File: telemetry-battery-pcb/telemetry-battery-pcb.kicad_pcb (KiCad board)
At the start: 2 copper layers, 95 x 65 mm, 110 parts, among them J1 Network Connector, J2 STDC14, J3 CONN_360410_MZC, J4 DS18B20, J5 CONN_360410_MZC, Q1 NMOS, Q2 PMOS, Q4 NMOS, SW1 SW_Push, U1 LD39050PU33R, U2 STM32G474RBT6, U3 SN65HVD230, U4 LTC2944, U5 XR76208, U6 M24C02-WMN, U7 TPS1HTC30-Q1, U8 DS2484Q, Y1 8MHz

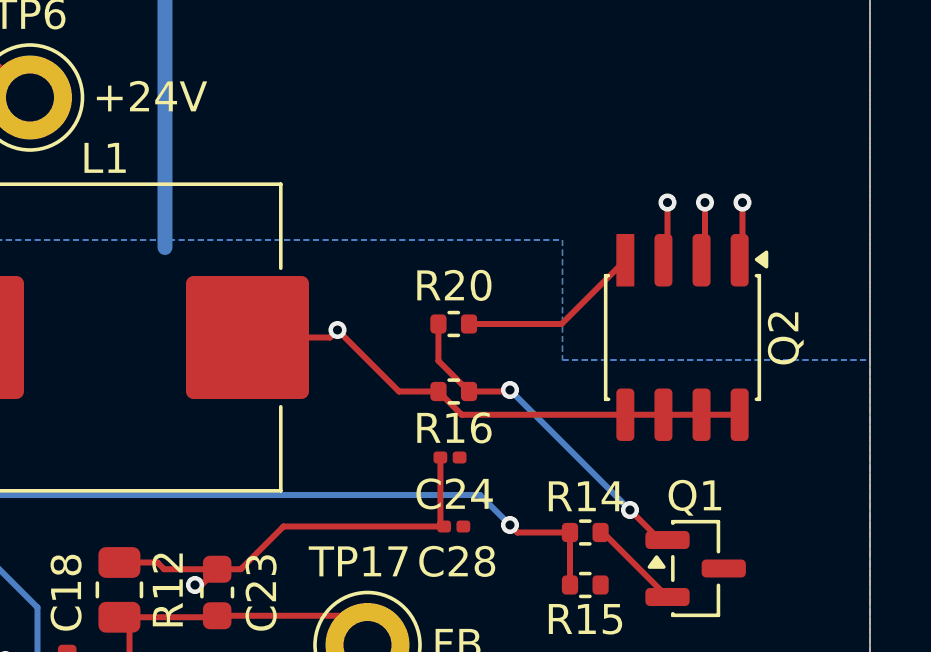
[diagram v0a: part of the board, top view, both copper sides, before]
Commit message: telemetry-battery-pcb: enlarge +5V net after coil
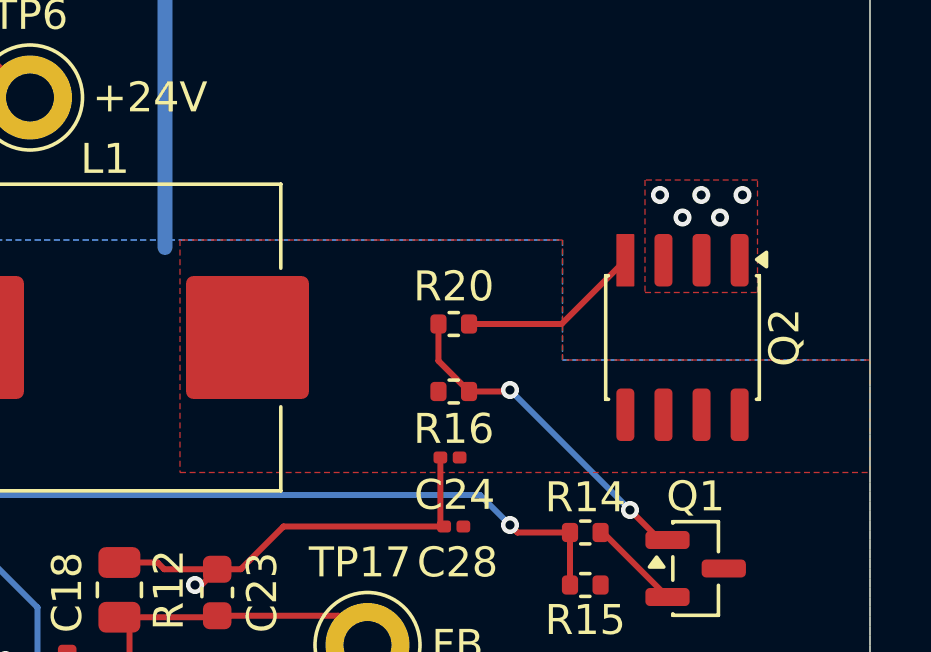
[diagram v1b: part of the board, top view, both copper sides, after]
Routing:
- net +5V: track 78.7 -> 62.7 mm, vias 4 -> 3
- net /5V_net: track 61.7 -> 56.2 mm, vias 4 -> 6
- added copper zone on F.Cu, net +5V
- added copper zone on F.Cu, net /5V_net
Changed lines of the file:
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@@
 	)
 	(segment
-		(start 121.5 50.25)
-		(end 121.75 50)
-		(width 0.2)
-		(layer "F.Cu")
-		(net 2)
-	)
-	(segment
 		(start 118.525 57.975)
 		(end 119.95 56.55)
@@
 	)
 	(segment
-		(start 135.155 52.825)
-		(end 125.89 52.825)
-		(width 0.2)
-		(layer "F.Cu")
-		(net 2)
-	)
-	(segment
-		(start 125.89 52.825)
-		(end 125.115 52.05)
-		(width 0.2)
-		(layer "F.Cu")
-		(net 2)
-	)
-	(segment
 		(start 93.5 29.75)
 		(end 92.68 30.57)
@@
 	)
 	(segment
-		(start 125.115 52.05)
-		(end 123.8 52.05)
-		(width 0.2)
-		(layer "F.Cu")
-		(net 2)
-	)
-	(segment
 		(start 114.48 57.75)
 		(end 115.75 57.75)
@@
 	)
 	(segment
-		(start 120.5 50.25)
-		(end 121.5 50.25)
-		(width 0.2)
-		(layer "F.Cu")
-		(net 2)
-	)
-	(segment
 		(start 91.22 32.335)
 		(end 92.53 32.335)
@@
 	)
 	(segment
-		(start 123.8 52.05)
-		(end 121.75 50)
-		(width 0.2)
-		(layer "F.Cu")
-		(net 2)
-	)
-	(segment
 		(start 120 50.25)
 		(end 120.5 50.25)
@@
 		(net 2)
 	)
-	(via
-		(at 121.75 50)
-		(size 0.6)
-		(drill 0.3)
-		(layers "F.Cu" "B.Cu")
-		(free yes)
-		(net 2)
-	)
 	(segment
 		(start 116 34.25)
@@
 	)
 	(segment
-		(start 132.75 45.75)
-		(end 132.75 47.54)
-		(width 0.2)
-		(layer "F.Cu")
-		(net 62)
-	)
-	(segment
 		(start 134 47.56)
 		(end 133.885 47.675)
@@
 	)
 	(segment
-		(start 135.25 45.75)
-		(end 135.25 47.58)
-		(width 0.2)
-		(layer "F.Cu")
-		(net 62)
-	)
-	(segment
-		(start 134 45.75)
-		(end 134 47.56)
-		(width 0.2)
-		(layer "F.Cu")
-		(net 62)
-	)
-	(segment
 		(start 132.75 47.54)
 		(end 132.615 47.675)
@@
 	)
 	(via
-		(at 132.75 45.75)
+		(at 133.875 45.5)
+		(size 0.6)
+		(drill 0.3)
+		(layers "F.Cu" "B.Cu")
+		(free yes)
+		(net 62)
+	)
+	(via
+		(at 132.5 45.5)
 		(size 0.6)
 		(drill 0.3)
@@
 	)
 	(via
-		(at 134 45.75)
+		(at 133.25 46.25)
+		(size 0.6)
+		(drill 0.3)
+		(layers "F.Cu" "B.Cu")
+		(free yes)
+		(net 62)
+	)
+	(via
+		(at 135.25 45.5)
 		(size 0.6)
 		(drill 0.3)
@@
 	)
 	(via
-		(at 135.25 45.75)
+		(at 134.5 46.25)
 		(size 0.6)
 		(drill 0.3)
@@
 			)
 		)
+	)
+	(zone
+		(net 62)
+		(net_name "/5V_net")
+		(layer "F.Cu")
+		(hatch edge 0.5)
+		(priority 8)
+		(connect_pads yes
+			(clearance 0.18)
+		)
+		(min_thickness 0.25)
+		(filled_areas_thickness no)
+		(fill yes
+			(thermal_gap 0.5)
+			(thermal_bridge_width 0.5)
+		)
+		(polygon
+			(pts
+				(xy 132 48.75) (xy 135.75 48.75) (xy 135.75 45) (xy 132 45)
+			)
+		)
+	)
+	(zone
+		(net 2)
+		(net_name "+5V")
+		(layer "F.Cu")
+		(hatch edge 0.5)
+		(priority 7)
+		(connect_pads yes
+			(clearance 0.18)
+		)
+		(min_thickness 0.25)
+		(filled_areas_thickness no)
+		(fill yes
+			(thermal_gap 0.5)
+			(thermal_bridge_width 0.5)
+		)
+		(polygon
+			(pts
+				(xy 139.5 51) (xy 129.25 51) (xy 129.25 47) (xy 116.5 47) (xy 116.5 54.75) (xy 139.5 54.75)
+			)
+		)

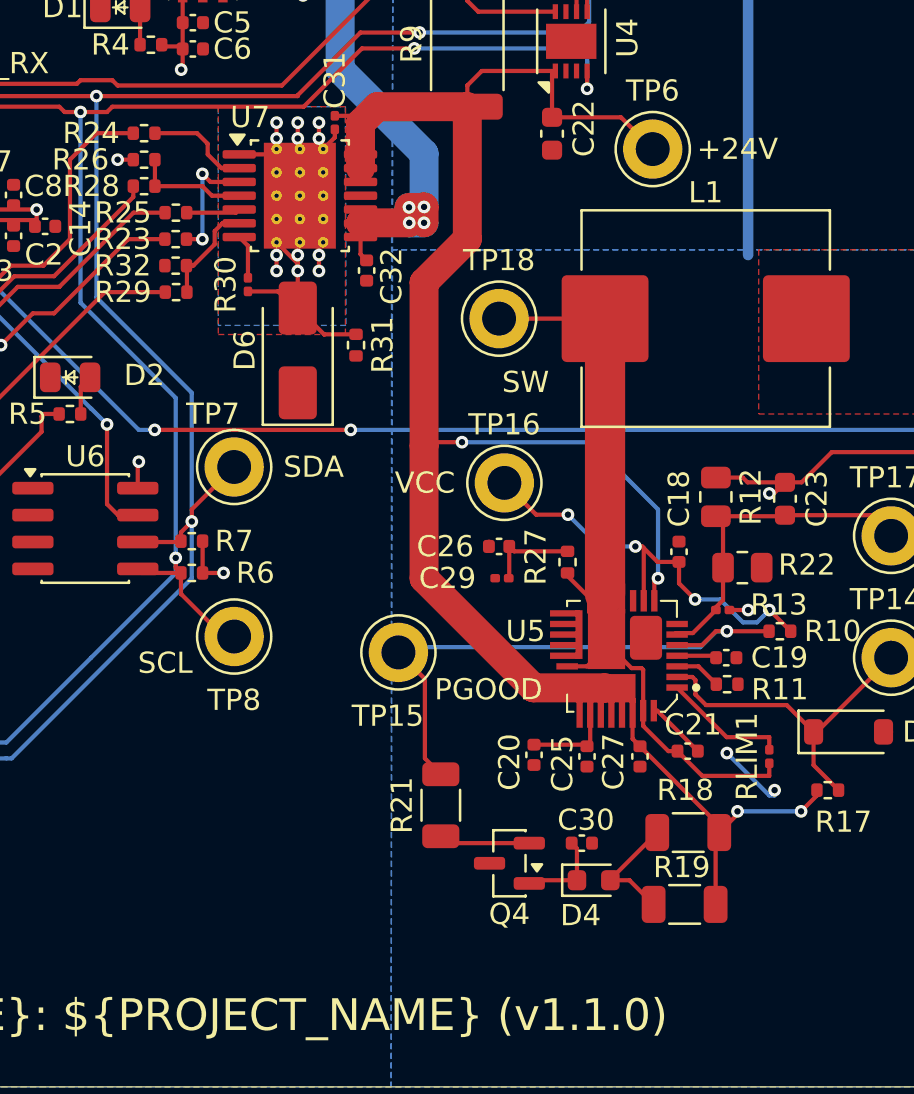
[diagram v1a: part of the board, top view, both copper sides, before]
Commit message: telemetry-battery-pcb: update JLCPCB component numbers
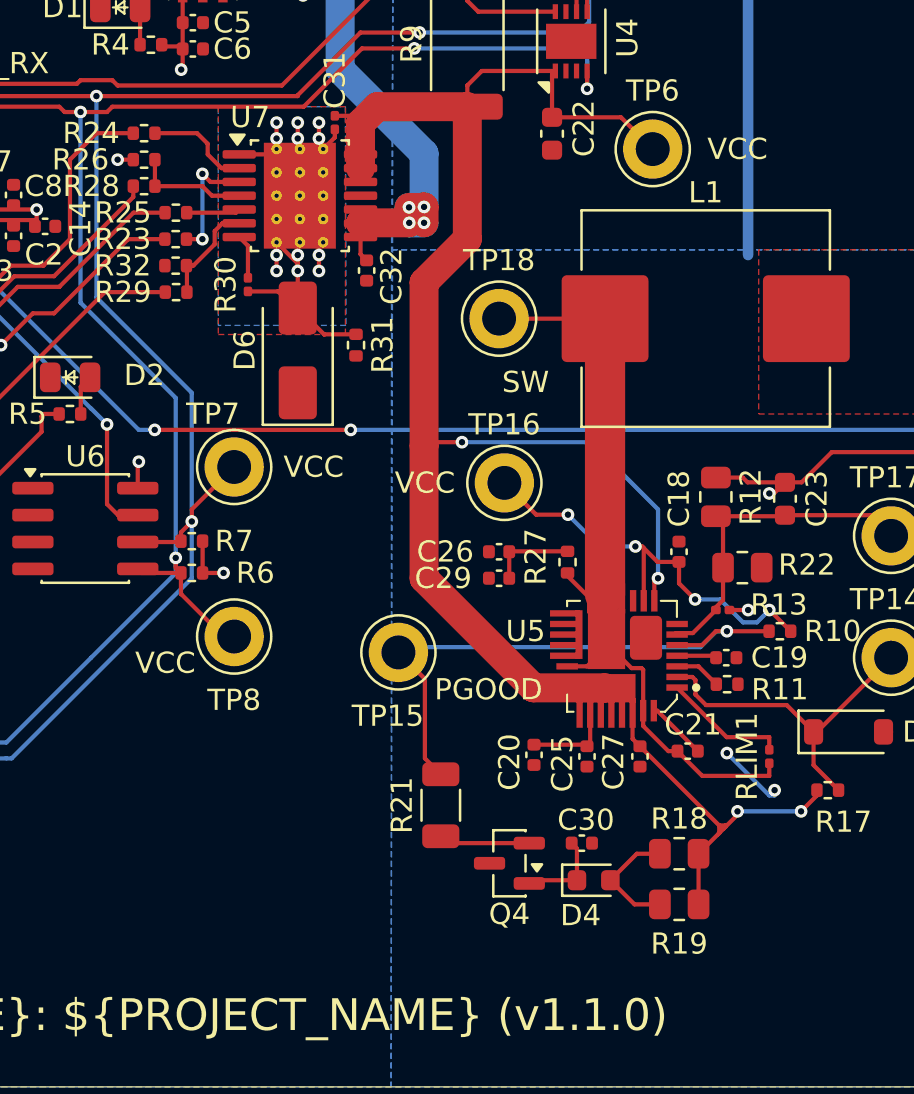
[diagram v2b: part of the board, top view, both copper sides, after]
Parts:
- C29: footprint Capacitor_SMD:C_0201_0603Metric -> Capacitor_SMD:C_0402_1005Metric
- R18, R19: value 3k -> 3.3k; footprint Resistor_SMD:R_1206_3216Metric -> Resistor_SMD:R_0805_2012Metric
- U7: value TPS1HTC30-Q1 -> ~
- moved R18 1.09 mm to (112.8, 75.5)
- moved R19 0.25 mm to (112.8, 77.9)
- moved C26 0.25 mm to (104.2, 61.2)
- moved C29 0.14 mm to (104.2, 62.5)
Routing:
- net +24V: track 93.3 -> 94.0 mm

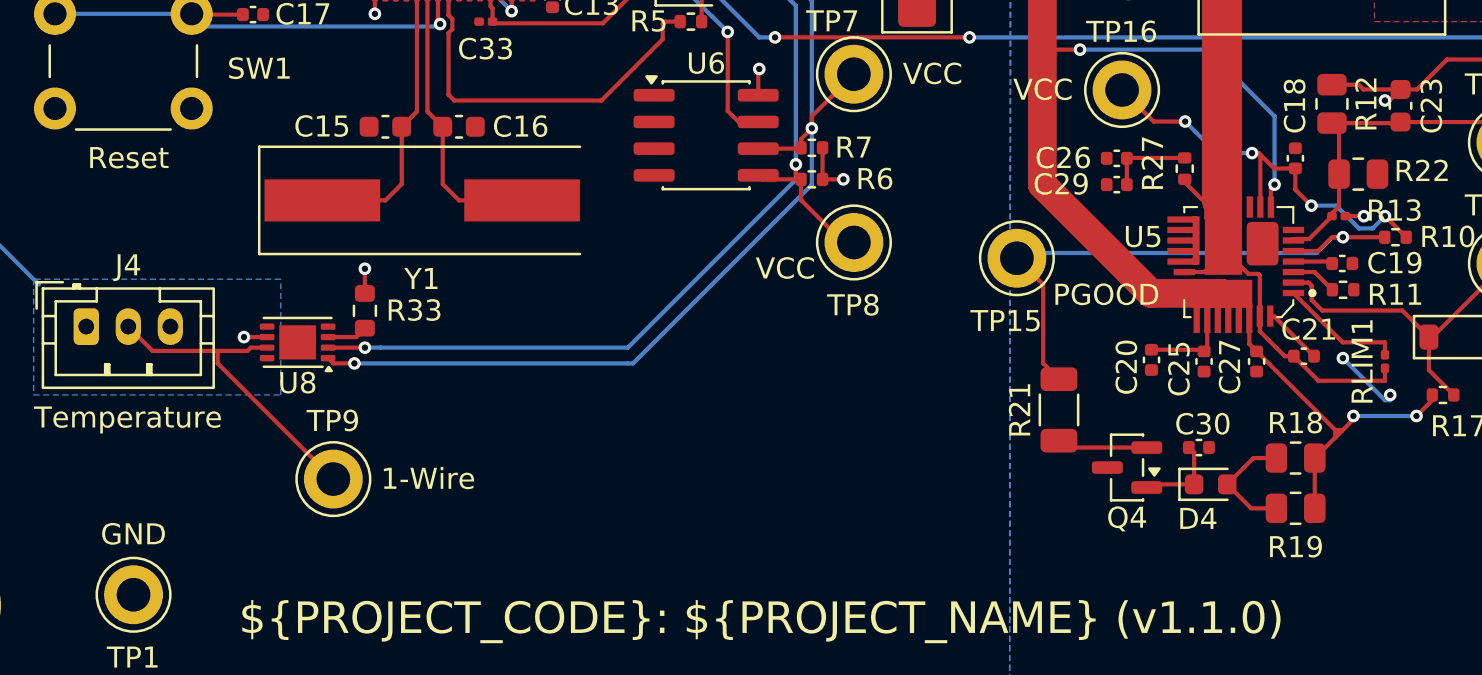
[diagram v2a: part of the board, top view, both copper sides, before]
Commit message: telemetry-battery-pcb: change DS2484 symbol
Using the DS2484R instead of DS2484Q as it is cheaper on JLCPCB.
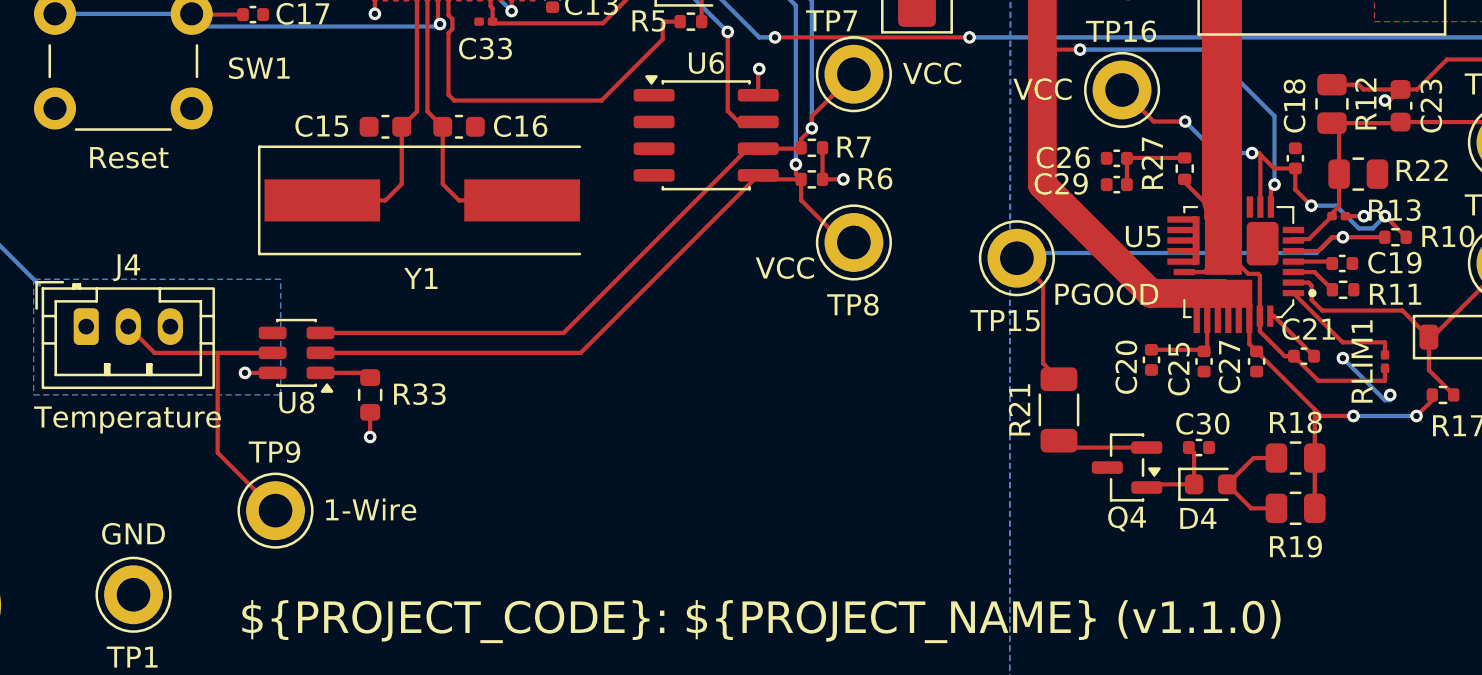
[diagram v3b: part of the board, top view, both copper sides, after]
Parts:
- U8: value DS2484Q -> DS2484R; footprint Package_DFN_QFN:Maxim_WSON-8-1EP_3x2mm_P0.5mm_EP1.75x1.63mm -> Package_TO_SOT_SMD:SOT-23-6
- moved R33 4.01 mm to (68.8, 72.5), turned to 90 degrees
- moved TP9 3.13 mm to (64.2, 78.0)
- moved U8 0.50 mm to (65.2, 70.5)
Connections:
- U8 pad 1: /SDA -> Net-(U8-~{SLPZ})
- U8 pad 3: Net-(U8-~{SLPZ}) -> /SDA
- U8 pad 4: unconnected-(U8-N.C.-Pad4) -> GND
- U8 pad 5: unconnected-(U8-N.C.-Pad5) -> /ONE_WIRE
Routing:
- net /SDA: track 98.5 -> 93.6 mm, vias 5 -> 4
- net /SCL: track 96.1 -> 94.2 mm, vias 5 -> 4
- net Net-(U8-~{SLPZ}): track 1.93 -> 2.46 mm
- net /ONE_WIRE: track 15.5 -> 16.0 mm

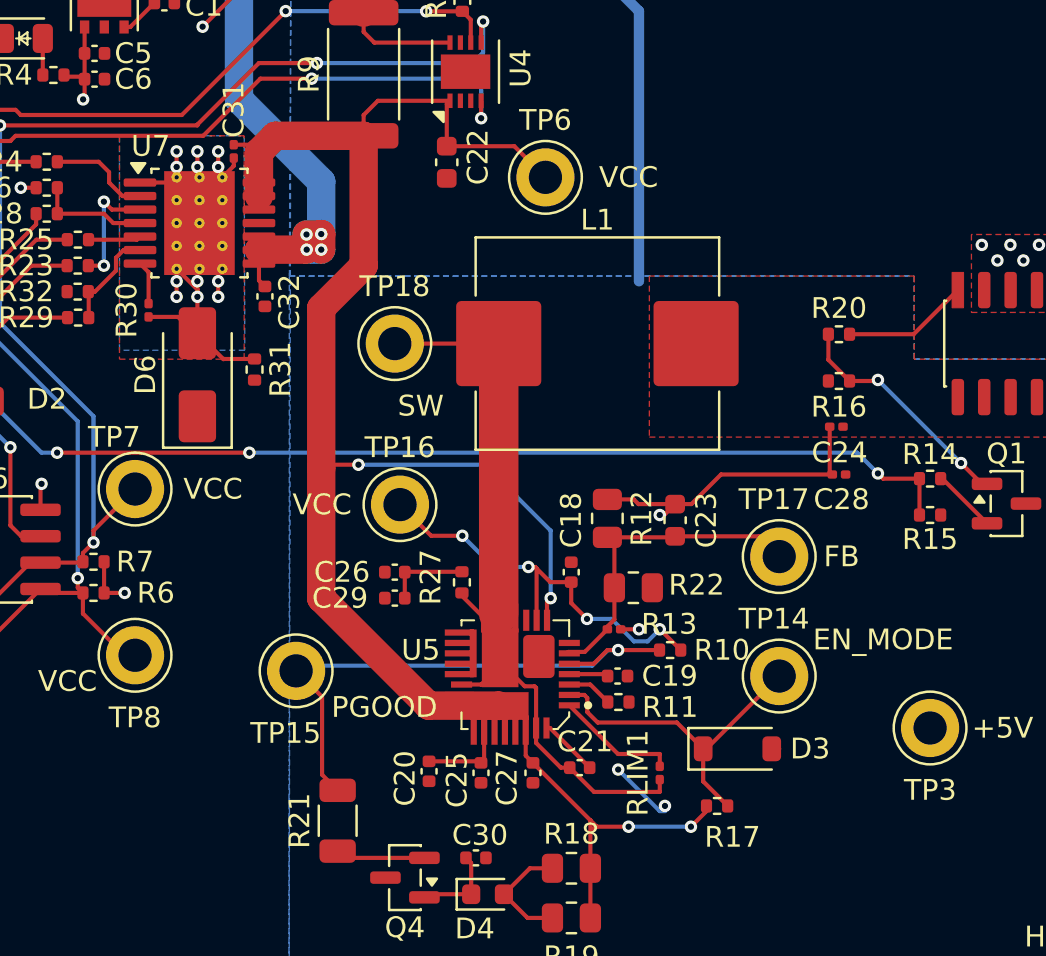
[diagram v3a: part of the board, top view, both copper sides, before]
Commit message: telemetry-battery-pcb : Update PCB
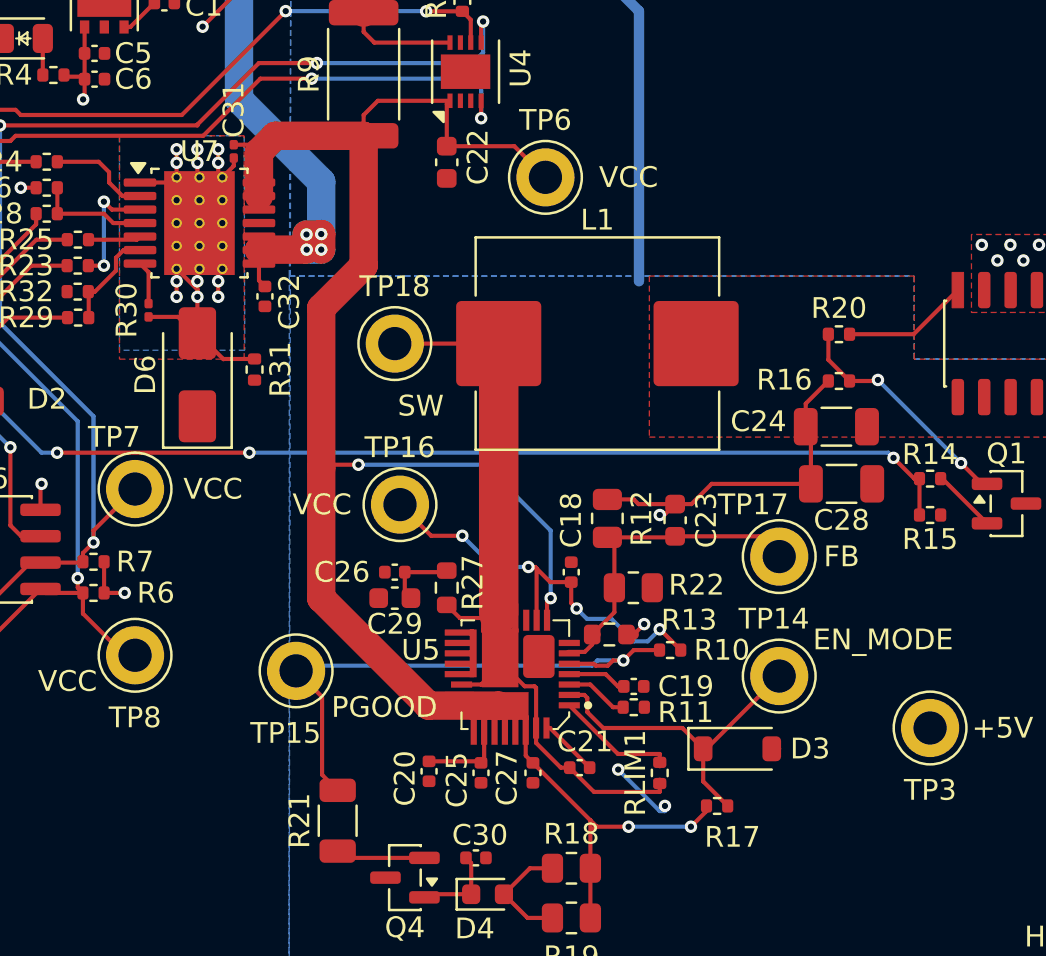
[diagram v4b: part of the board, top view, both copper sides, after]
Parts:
- C24, C28: footprint Capacitor_SMD:C_0201_0603Metric -> Capacitor_SMD:C_1206_3216Metric
- C29: footprint Capacitor_SMD:C_0402_1005Metric -> Capacitor_SMD:C_0603_1608Metric
- R13: footprint Resistor_SMD:R_0201_0603Metric -> Resistor_SMD:R_0603_1608Metric
- R27: footprint Resistor_SMD:R_0402_1005Metric -> Resistor_SMD:R_0603_1608Metric
- RLIM1: footprint Resistor_SMD:R_0201_0603Metric -> Resistor_SMD:R_0402_1005Metric
- U7: value ~ -> Tps1htc; footprint Package_SO:Texas_HTSSOP-14-1EP_4.4x5mm_P0.65mm_EP3.4x5mm_Mask3.155x3.255mm_ThermalVias -> Exocet:Tps1htc_Exocet_Texas_HTSSOP-14-1EP_4.4x5mm_P0.65mm_EP3.4x5mm_Mask3.155x3.255mm_ThermalVias
- moved C19 0.93 mm to (115.8, 66.8)
- moved R11 0.78 mm to (115.8, 67.8)
- moved R27 0.77 mm to (106.8, 62.0)
- moved C28 0.47 mm to (125.8, 57.0)
- moved R13 0.34 mm to (114.6, 64.2)
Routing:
- net +5V: track 62.7 -> 64.8 mm
- net Net-(U5-SS): track 1.88 -> 2.87 mm
- net Net-(U5-TON): track 2.20 -> 3.04 mm
- net Net-(C26-Pad2): track 4.04 -> 3.36 mm
